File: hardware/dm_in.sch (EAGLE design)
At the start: 56 parts, among them IC102 MAX487CSA, IC2 LTV-356T, IC3 78SO05, IC4 LTV-354T, IC6 ATMEGA328-A, X1 AKL_183-02, X2 AKL_183-02, X3 AKL_183-04, X4 AKL_183-02, X5 AKL_183-02, X6 AKL_183-02, X7 AKL_183-02

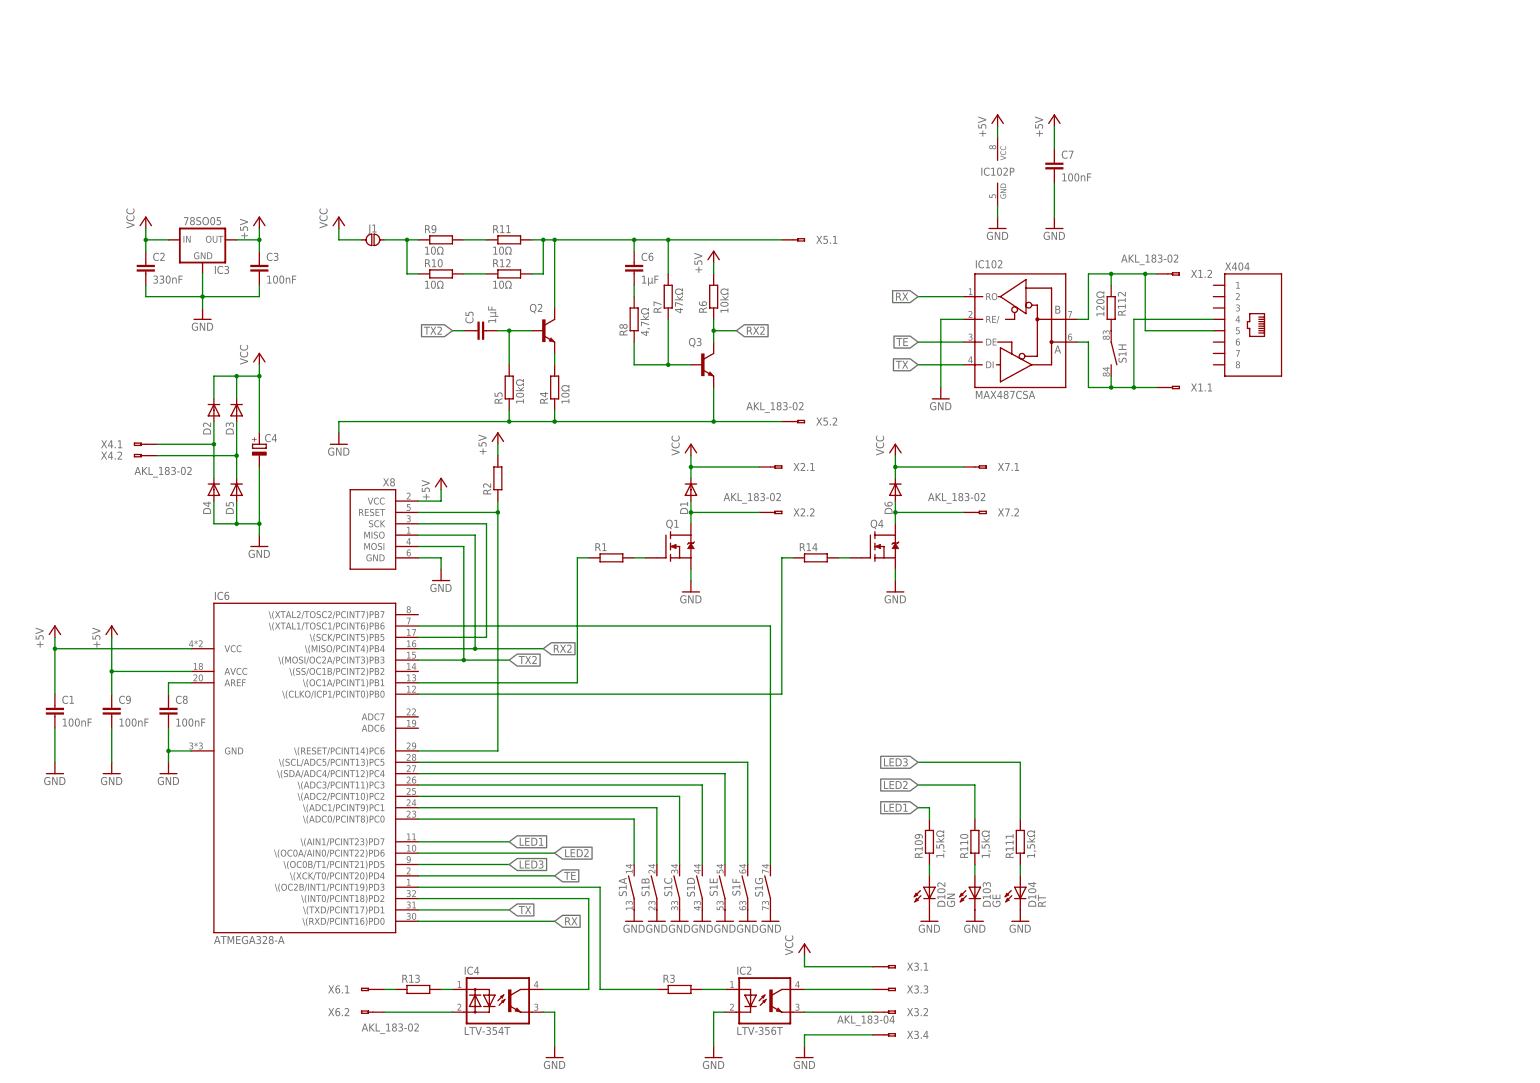
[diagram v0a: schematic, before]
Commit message: Detailverbesserungen an Türmodul
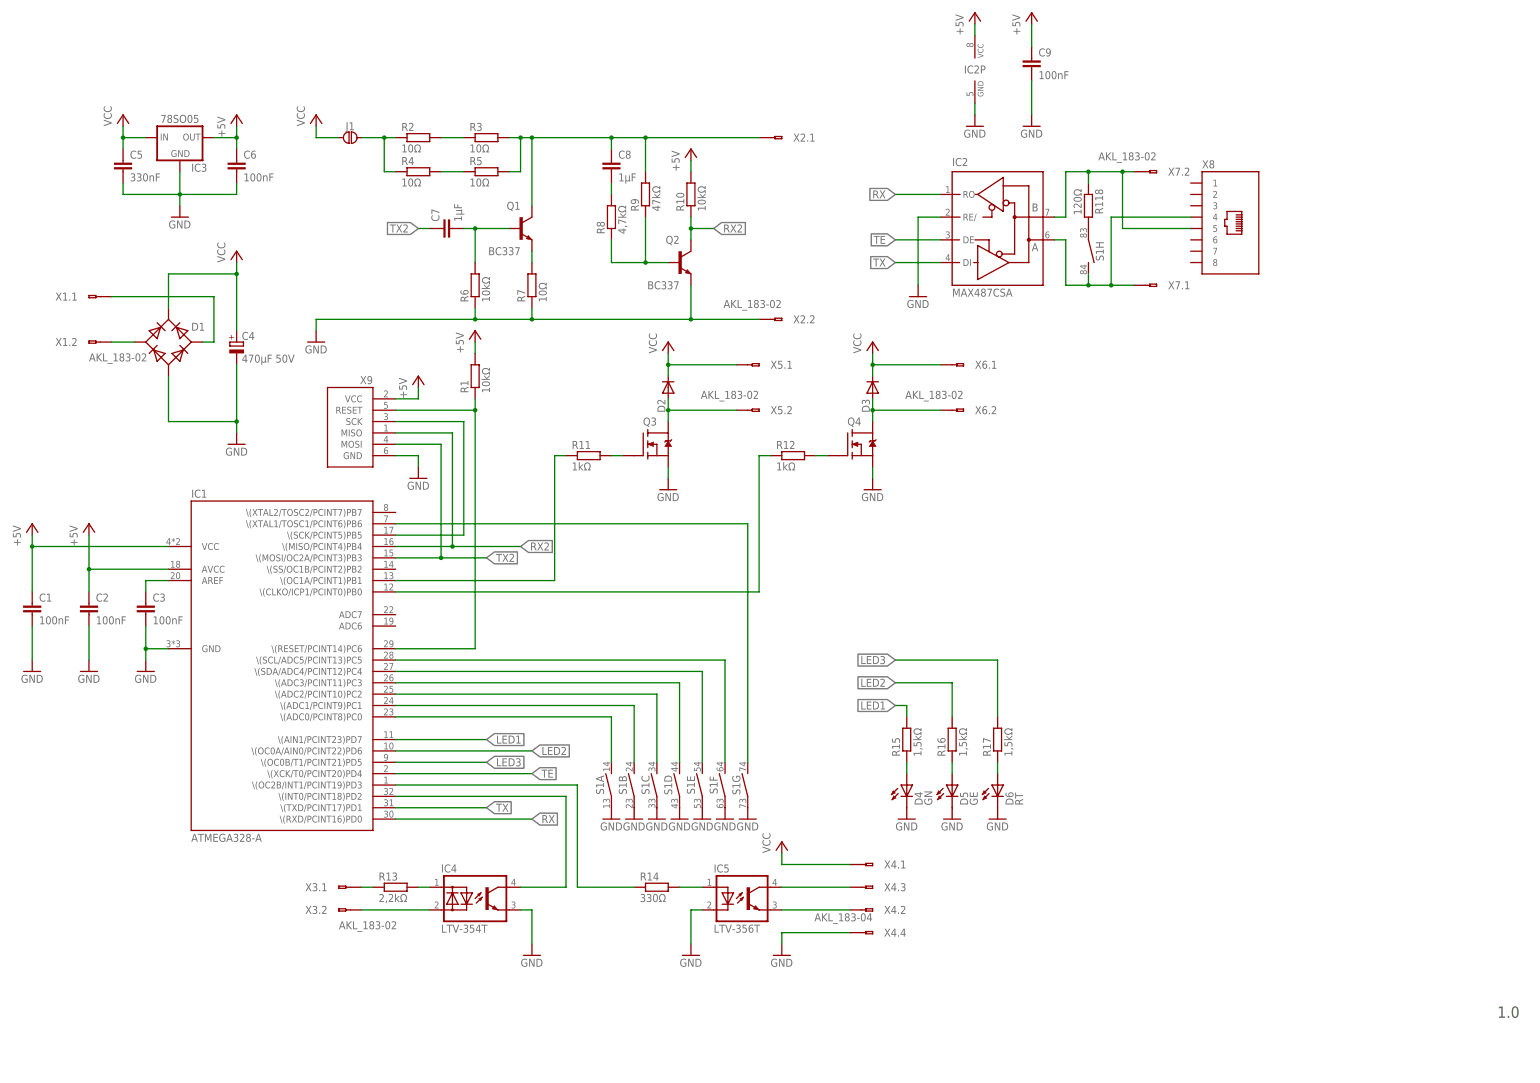
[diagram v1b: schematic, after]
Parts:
- removed D102: GN, led:LED_0805
- removed D103: GE, led:LED_0805
- removed D104: RT, led:LED_0805
- removed IC102: MAX487CSA, ic-wandler:MAX487CSA
- removed IC6: ATMEGA328-A, ic-mcu:ATMEGA328-A
- removed R109, R110, R111: 1,5kΩ, passiv:R_0603
- removed R112: 120Ω, passiv:R_0805
- removed X404: (no value), stecker:8P8C
- added IC1: ATMEGA328-A, ic-mcu:ATMEGA328-A
- added IC5: LTV-356T, ic-optokoppler:LTV-356T
- added R118: 120Ω, passiv:R_0805
- added R15, R16, R17: 1,5kΩ, passiv:R_0603
- added X9: (no value), stecker:ISP-AVR6
- C2: value 330nF -> 100nF; device passiv:C_0805 -> passiv:C_0603
- C3: device passiv:C_0805 -> passiv:C_0603
- C4: value (none) -> 470μF 50V
- C5: value 1μF -> 330nF; device passiv:C_1206 -> passiv:C_0805
- C6: value 1μF -> 100nF; device passiv:C_1206 -> passiv:C_0805
- C7, C8: value 100nF -> 1μF; device passiv:C_0603 -> passiv:C_1206
- D1: device diode:DIODE-SOD123 -> diode:GLEICHRICHTER-SDIP
- D4: value (none) -> GN; device diode:DIODE-SOD123 -> led:LED_0805
- D5: value (none) -> GE; device diode:DIODE-SOD123 -> led:LED_0805
- D6: value (none) -> RT; device diode:DIODE-SOD123 -> led:LED_0805
- IC2: value LTV-356T -> MAX487CSA; device ic-optokoppler:LTV-356T -> ic-wandler:MAX487CSA
- Q1: value (none) -> BC337; device transistor:N-MOS-SOT23-GSD -> transistor:NPN-SOT23-BEC
- Q2: value (none) -> BC337
- Q3: device transistor:NPN-SOT23-BEC -> transistor:N-MOS-SOT23-GSD
- R1: value (none) -> 10kΩ
- R10: value 10Ω -> 10kΩ; device passiv:R_1206 -> passiv:R_0603
- R11, R12: value 10Ω -> 1kΩ; device passiv:R_1206 -> passiv:R_0603
- R13: value (none) -> 2,2kΩ
- R14: value (none) -> 330Ω
- R2, R3: value (none) -> 10Ω; device passiv:R_0603 -> passiv:R_1206
- R5: value 10kΩ -> 10Ω; device passiv:R_0603 -> passiv:R_1206
- R7: value 47kΩ -> 10Ω; device passiv:R_0603 -> passiv:R_1206
- R9: value 10Ω -> 47kΩ; device passiv:R_1206 -> passiv:R_0603
- X3: value AKL_183-04 -> AKL_183-02; device anschluss:AKL_183-04 -> anschluss:AKL_183-02
- X4: value AKL_183-02 -> AKL_183-04; device anschluss:AKL_183-02 -> anschluss:AKL_183-04
- X8: device stecker:ISP-AVR6 -> stecker:8P8C
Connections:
- net +5V: now also C2.1, C6.1, IC1.AVCC, IC1.VCC, IC2P.VCC, R1.2, R10.2, X9.VCC; no longer C3.1, C7.1, IC102P.VCC, IC6.AVCC, IC6.VCC, R2.2, R6.2, X8.VCC
- net GND: now also C5.2, C6.2, D1.-, D4.C, D5.C, D6.C, IC1.GND, IC2A.RE/, IC2P.GND, IC5.K, Q2.E, Q3.S, R6.1, R7.1, X2.2.A, X4.4.A, X9.GND; no longer C7.2, C8.2, D102.C, D103.C, D104.C, D4.A, D5.A, IC102A.RE/, IC102P.GND, IC2.K, IC6.GND, Q1.S, Q3.E, R4.1, R5.1, X3.4.A, X5.2.A, X8.GND
- net LED1: now also IC1.\(AIN1/PCINT23)PD7, R15.2; no longer IC6.\(AIN1/PCINT23)PD7, R109.2
- net LED2: now also IC1.\(OC0A/AIN0/PCINT22)PD6, R16.2; no longer IC6.\(OC0A/AIN0/PCINT22)PD6, R110.2
- net LED3: now also IC1.\(OC0B/T1/PCINT21)PD5, R17.2; no longer IC6.\(OC0B/T1/PCINT21)PD5, R111.2
- net N$1: now also IC1.\(INT0/PCINT18)PD2; no longer IC6.\(INT0/PCINT18)PD2
- net N$10: now also IC1.\(OC2B/INT1/PCINT19)PD3, R14.1; no longer IC6.\(OC2B/INT1/PCINT19)PD3, R3.1
- net N$11: now also IC5.A, R14.2; no longer IC2.A, R3.2
- net N$12: now also R2.1, R4.1; no longer R10.1, R9.1
- net N$13: now also R2.2, R3.1; no longer R11.1, R9.2
- net N$14: now also X3.1.A; no longer X6.1.A
- net N$16: now also Q1.E, R7.2; no longer Q2.E, R4.2
- net N$17: now also C7.2, Q1.B, R6.2; no longer C5.2, Q2.B, R5.2
- net N$18: now also Q2.B, R9.1; no longer Q3.B, R7.1
- net N$19: now also C8.2; no longer C6.2
- net N$2: now also X3.2.A; no longer X6.2.A
- net N$20: now also D1.AC2, X1.1.A; no longer D2.A, D4.K, X4.1.A
- net N$21: now also C8.1, Q1.C, R3.2, R5.2, R9.2, X2.1.A; no longer C6.1, Q2.C, R11.2, R12.2, R7.2, X5.1.A
- net N$22: now also D1.AC1, X1.2.A; no longer D3.A, D5.K, X4.2.A
- net N$23: now also R4.2, R5.1; no longer R10.2, R12.1
- net N$24: now also R12.2; no longer R14.2
- net N$25: now also D3.A, X6.2.A; no longer D6.A, X7.2.A
- net N$26: now also IC1.\(CLKO/ICP1/PCINT0)PB0, R12.1; no longer IC6.\(CLKO/ICP1/PCINT0)PB0, R14.1
- net N$27: now also IC2A.B, R118.1, X7.2.A, X8.5; no longer IC102A.B, R112.1, X1.2.A, X404.5
- net N$28: now also IC1.\(ADC0/PCINT8)PC0; no longer IC6.\(ADC0/PCINT8)PC0
- net N$29: now also IC1.\(ADC1/PCINT9)PC1; no longer IC6.\(ADC1/PCINT9)PC1
- net N$3: now also IC2A.A, X7.1.A, X8.4; no longer IC102A.A, X1.1.A, X404.4
- net N$30: now also IC1.\(ADC2/PCINT10)PC2; no longer IC6.\(ADC2/PCINT10)PC2
- net N$31: now also IC1.\(ADC3/PCINT11)PC3; no longer IC6.\(ADC3/PCINT11)PC3
- net N$32: now also IC1.\(SDA/ADC4/PCINT12)PC4; no longer IC6.\(SDA/ADC4/PCINT12)PC4
- net N$33: now also R118.2; no longer R112.2
- net N$34: now also IC1.\(SCL/ADC5/PCINT13)PC5; no longer IC6.\(SCL/ADC5/PCINT13)PC5
- net N$35: now also IC1.\(XTAL1/TOSC1/PCINT6)PB6; no longer IC6.\(XTAL1/TOSC1/PCINT6)PB6
- net N$36: now also D6.A, R17.1; no longer D104.A, R111.1
- net N$38: now also IC1.\(SCK/PCINT5)PB5, X9.SCK; no longer IC6.\(SCK/PCINT5)PB5, X8.SCK
- net N$39: now also C3.1, IC1.AREF; no longer C8.1, IC6.AREF
- net N$4: now also IC1.\(RESET/PCINT14)PC6, R1.1, X9.RESET; no longer IC6.\(RESET/PCINT14)PC6, R2.1, X8.RESET
- net N$5: now also IC1.\(OC1A/PCINT1)PB1, R11.1; no longer IC6.\(OC1A/PCINT1)PB1, R1.1
- net N$6: now also Q3.G, R11.2; no longer Q1.G, R1.2
- net N$62: now also D4.A, R15.1; no longer D102.A, R109.1
- net N$63: now also D5.A, R16.1; no longer D103.A, R110.1
- net N$7: now also D2.A, Q3.D, X5.2.A; no longer D1.A, Q1.D, X2.2.A
- net N$8: now also IC5.E, X4.2.A; no longer IC2.E, X3.2.A
- net N$9: now also IC5.C, X4.3.A; no longer IC2.C, X3.3.A
- net RX: now also IC1.\(RXD/PCINT16)PD0, IC2A.RO; no longer IC102A.RO, IC6.\(RXD/PCINT16)PD0
- net RX2: now also IC1.\(MISO/PCINT4)PB4, Q2.C, R10.1, X9.MISO; no longer IC6.\(MISO/PCINT4)PB4, Q3.C, R6.1, X8.MISO
- net TE: now also IC1.\(XCK/T0/PCINT20)PD4, IC2A.DE; no longer IC102A.DE, IC6.\(XCK/T0/PCINT20)PD4
- net TX: now also IC1.\(TXD/PCINT17)PD1, IC2A.DI; no longer IC102A.DI, IC6.\(TXD/PCINT17)PD1
- net TX2: now also C7.1, IC1.\(MOSI/OC2A/PCINT3)PB3, X9.MOSI; no longer C5.1, IC6.\(MOSI/OC2A/PCINT3)PB3, X8.MOSI
- net VCC: now also C5.1, D1.+, X4.1.A, X5.1.A, X6.1.A; no longer C2.1, D1.K, D6.K, X2.1.A, X3.1.A, X7.1.A
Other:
- note added: "1.0"
- moved on the sheet: C1, C2, C3, C4, C5, C6, C7, C8, C9, D2, D3, IC3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
